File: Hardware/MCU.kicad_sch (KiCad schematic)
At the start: 53 parts, among them J1 Serial Wire Debug(SWD), J2 Conn_01x07 USART2, J3 Conn_01x07 LPUART1, J4 Conn_01x08 SPI1, J5 Conn_01x05 I2C, SW3 SW_Push, U6 STM32L010F4Px

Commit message: PCB is done???
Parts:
- J1: value Serial Wire Debug(SWD) -> SWD
- J2: footprint Connector_PinHeader_2.54mm:PinHeader_1x07_P2.54mm_Vertical -> Connector_PinHeader_2.54mm:PinHeader_1x07_P2.54mm_Vertical_SMD_Pin1Left
- J3, J4, J5: now not fitted; now left out of the parts list
- SW3: value SW_Push -> Reset; footprint (none) -> Button_Switch_SMD:SW_Push_1P1T_NO_6x6mm_H9.5mm
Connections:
- net PA5 A5 is gone; now on net IN Signal: JP14.2 (B), JP7.2 (C), U6.11 (PA5)
- net PA6 A6 is gone; now on net IN Ref: JP11.2 (B), JP31.2 (B), JP8.2 (C), U6.12 (PA6)
- net USART2_CK is gone; now on net PA4 A4: J2.6 (Pin_6), JP23.1 (A), JP24.1 (A)
- net USART2_CTS is gone; now on net PA0 A0: J2.5 (Pin_5), JP28.1 (A), JP29.1 (A)
- net USART2_RTS is gone; now on net PA1 A1: J2.4 (Pin_4), JP30.1 (A)
- net USART2_RX is gone; now on net PA3 A3: J2.3 (Pin_3), JP20.1 (A), JP21.1 (A), JP22.1 (A)
- net USART2_TX is gone; now on net PA2 A2: J2.2 (Pin_2), JP25.1 (A), JP26.1 (A), JP27.1 (A)
- no-connect marks 1 -> 5
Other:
- moved on the sheet: J2

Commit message: PCB layed-out
- [x] headphone jack
- [x] UART header
- [x] Only one power trace with sub optimal return path
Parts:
- J1: footprint Connector_PinHeader_2.54mm:PinHeader_1x06_P2.54mm_Vertical -> Connector_PinHeader_2.54mm:PinHeader_1x06_P2.54mm_Vertical_SMD_Pin1Left
- J2: value Conn_01x07 USART2 -> USART2
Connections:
- net IN Ref: now also JP14.2 (B), JP7.2 (C), U6.11 (PA5); no longer JP11.2 (B), JP31.2 (B), JP8.2 (C), U6.12 (PA6)
- net IN Signal: now also JP11.2 (B), JP31.2 (B), JP8.2 (C), U6.12 (PA6); no longer JP14.2 (B), JP7.2 (C), U6.11 (PA5)
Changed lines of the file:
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@@
-		)
-	)
-	(hierarchical_label "IN Ref"
-		(shape input)
-		(at 77.47 95.25 180)
-		(effects
-			(font
-				(size 1.27 1.27)
-			)
-			(justify right)
 		)
 	)
@@
 		)
 	)
+	(hierarchical_label "IN Ref"
+		(shape input)
+		(at 77.47 91.44 180)
+		(effects
+			(font
+				(size 1.27 1.27)
+			)
+			(justify right)
+		)
+	)
 	(hierarchical_label "+3V3"
 		(shape input)
@@
 	(hierarchical_label "IN Signal"
 		(shape input)
-		(at 77.47 91.44 180)
+		(at 77.47 95.25 180)
 		(effects
 			(font
@@
 			)
 		)
-		(property "Value" "Conn_01x07 USART2"
+		(property "Value" "USART2"
 			(at 62.23 139.6999 0)
 			(effects
@@
 			)
 		)
-		(property "Footprint" "Connector_PinHeader_2.54mm:PinHeader_1x06_P2.54mm_Vertical"
+		(property "Footprint" "Connector_PinHeader_2.54mm:PinHeader_1x06_P2.54mm_Vertical_SMD_Pin1Left"
 			(at 96.52 69.85 0)
 			(effects

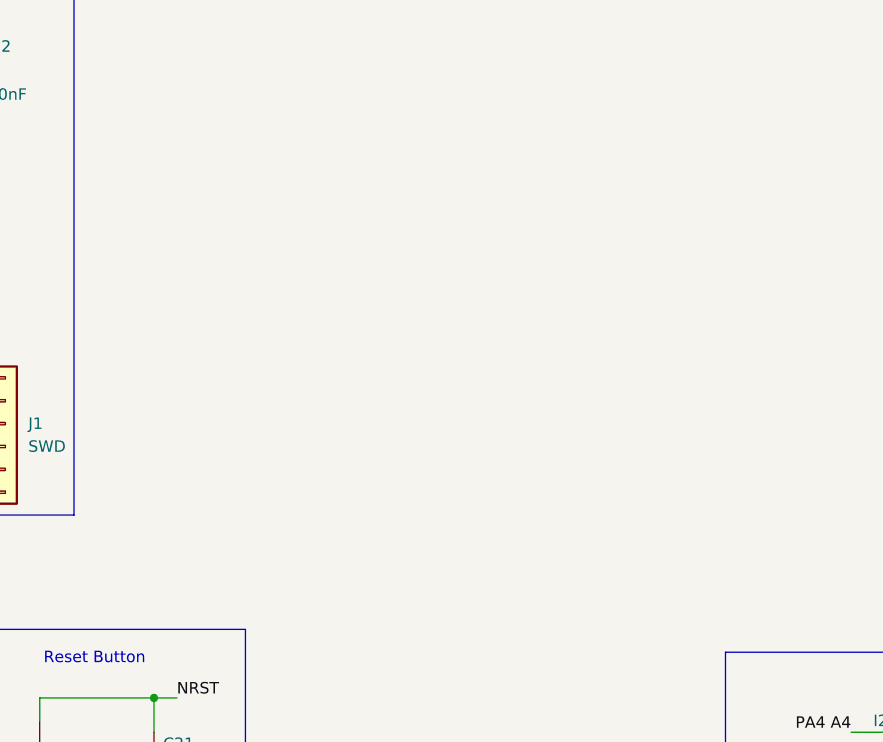
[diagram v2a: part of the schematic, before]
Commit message: added four leds
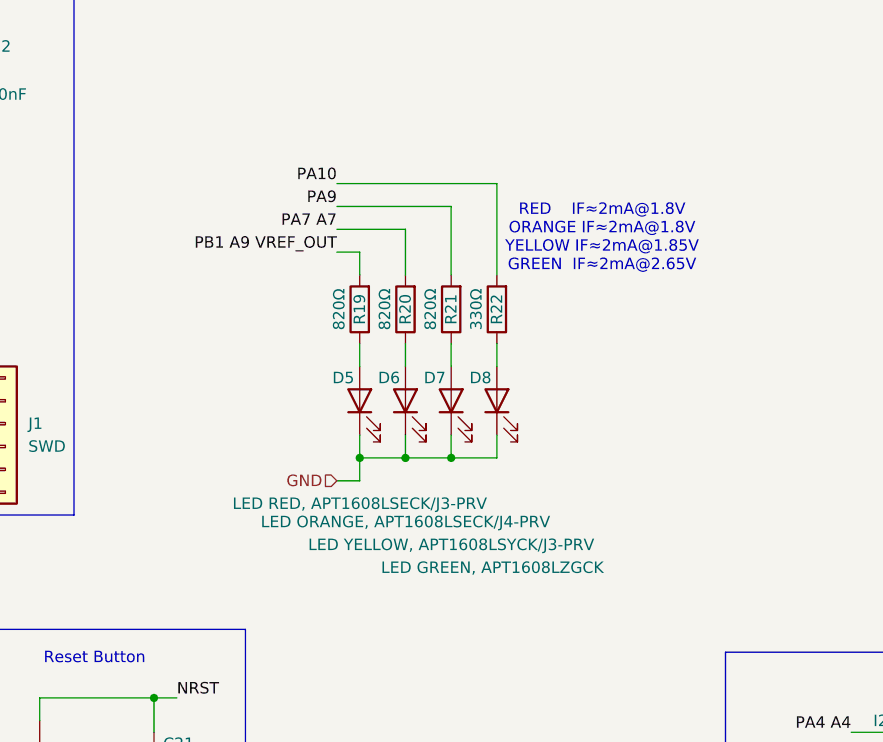
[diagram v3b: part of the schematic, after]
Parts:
- added D5: LED RED, APT1608LSECK/J3-PRV, LED_SMD:LED_0603_1608Metric_Pad1.05x0.95mm_HandSolder, symbol Device:LED
- added D6: LED ORANGE, APT1608LSECK/J4-PRV, LED_SMD:LED_0603_1608Metric_Pad1.05x0.95mm_HandSolder, symbol Device:LED
- added D7: LED YELLOW, APT1608LSYCK/J3-PRV, LED_SMD:LED_0603_1608Metric_Pad1.05x0.95mm_HandSolder, symbol Device:LED
- added D8: LED GREEN, APT1608LZGCK, LED_SMD:LED_0603_1608Metric_Pad1.05x0.95mm_HandSolder, symbol Device:LED
- added R19, R20, R21: 820Ω, Resistor_SMD:R_0402_1005Metric_Pad0.72x0.64mm_HandSolder, symbol Device:R
- added R22: 330Ω, Resistor_SMD:R_0402_1005Metric_Pad0.72x0.64mm_HandSolder, symbol Device:R
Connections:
- net GND: now also D5.1 (K), D6.1 (K), D7.1 (K), D8.1 (K)
- net PA10: now also R22.2
- net PA7 A7: now also R20.2
- net PA9: now also R21.2
- net PB1 A9 VREF_OUT: now also R19.2
- new net: D8.2 (A), R22.1
- new net: D5.2 (A), R19.1
- new net: D7.2 (A), R21.1
- new net: D6.2 (A), R20.1
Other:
- note added: "RED IF≈2mA@1.8V ORANGE IF≈2mA@1.8V YELLOW IF≈2mA@1.85V GREEN IF≈2mA@2.65V"

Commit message: closed KiCad
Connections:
- net PA7 A7: now also R19.2; no longer R20.2
- net PB1 A9 VREF_OUT: now also R20.2; no longer R19.2
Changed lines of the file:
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@@
+	(wire
+		(pts
+			(xy 133.35 48.26) (xy 135.89 48.26)
+		)
+		(stroke
+			(width 0)
+			(type default)
+		)
+	)
 	(wire
 		(pts
@@
 	(wire
 		(pts
-			(xy 133.35 48.26) (xy 140.97 48.26)
-		)
-		(stroke
-			(width 0)
-			(type default)
-		)
-	)
-	(wire
-		(pts
 			(xy 52.07 140.97) (xy 54.61 140.97)
 		)
@@
 	(wire
 		(pts
+			(xy 140.97 50.8) (xy 140.97 53.34)
+		)
+		(stroke
+			(width 0)
+			(type default)
+		)
+	)
+	(wire
+		(pts
 			(xy 222.25 114.3) (xy 222.25 110.49)
 		)
@@
 	(wire
 		(pts
-			(xy 140.97 48.26) (xy 140.97 53.34)
-		)
-		(stroke
-			(width 0)
-			(type default)
-		)
-	)
-	(wire
-		(pts
 			(xy 59.69 102.87) (xy 62.23 102.87)
 		)
@@
 	(wire
 		(pts
-			(xy 133.35 50.8) (xy 135.89 50.8)
-		)
-		(stroke
-			(width 0)
-			(type default)
-		)
-	)
-	(wire
-		(pts
 			(xy 64.77 171.45) (xy 67.31 171.45)
 		)
@@
 	(wire
 		(pts
-			(xy 135.89 50.8) (xy 135.89 53.34)
+			(xy 135.89 48.26) (xy 135.89 53.34)
 		)
 		(stroke
@@
 		)
 		(stroke
+			(width 0)
+			(type default)
+		)
+	)
+	(wire
+		(pts
+			(xy 133.35 50.8) (xy 140.97 50.8)
+		)
+		(stroke
